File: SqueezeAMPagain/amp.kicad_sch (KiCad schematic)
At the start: 52 parts, among them U1 TAS5756M

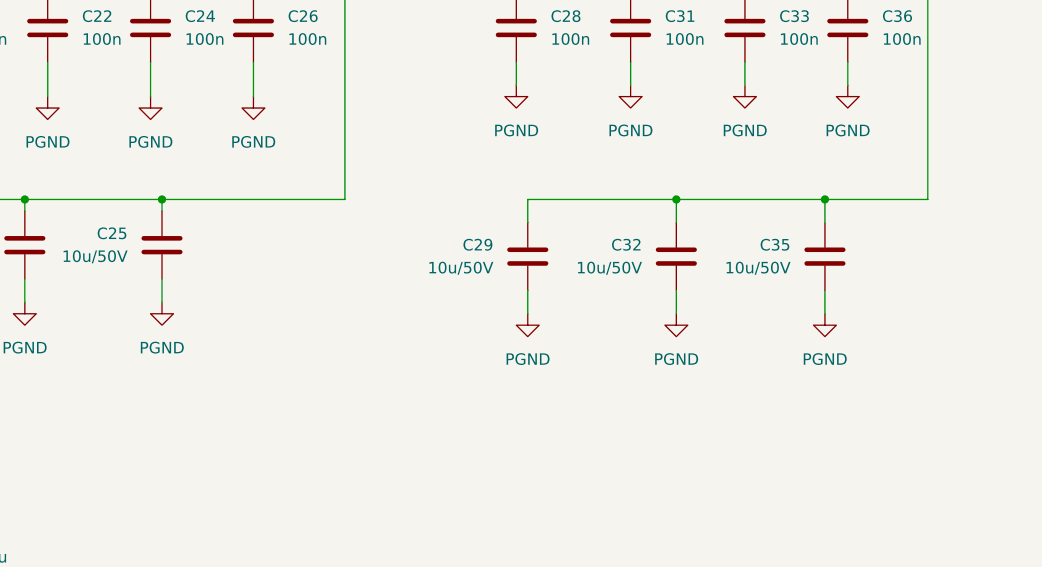
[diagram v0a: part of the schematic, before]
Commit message: Update SqueezeAMPagain.kicad_pcb, SqueezeAMPagain.kicad_prl, SqueezeAMPagain.kicad_pro, and 5 more files
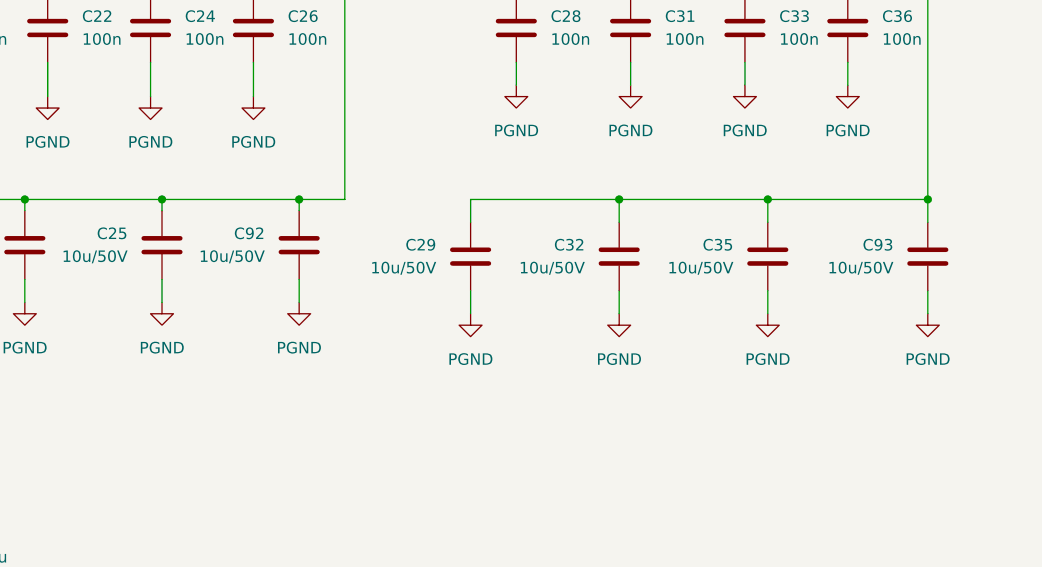
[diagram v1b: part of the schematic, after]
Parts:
- added C92, C93: 10u/50V, Capacitor_SMD:C_1206_3216Metric, symbol Device:C
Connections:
- net PGND: now also C92.2, C93.2
- net PVDD: now also C92.1, C93.1
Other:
- moved on the sheet: C29, C32, C35

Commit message: Update SqueezeAMPagain.kicad_pcb, SqueezeAMPagain.kicad_prl, SqueezeAMPagain.kicad_pro, and 11 more files
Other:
- title: Amplifier section -> SqueezeAMP_{again}
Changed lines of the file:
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@@
 	(paper "A4")
 	(title_block
-		(title "Amplifier section")
+		(title "SqueezeAMP_{again}")
+		(date "2024-08-23")
+		(rev "1.0")
 	)
 	(junction

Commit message: Update SqueezeAMPagain.kicad_pcb, SqueezeAMPagain.kicad_prl, SqueezeAMPagain.kicad_pro, and 4 more files
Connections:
- net +3.3V_{SW}: no longer C1.1, C3.1, U1.35 (CPVSS)
- new net: C1.1, C3.1, U1.35 (CPVSS)
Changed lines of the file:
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@@
 	)
 	(junction
-		(at 17.78 110.49)
-		(diameter 0)
-		(color 0 0 0 0)
-	)
-	(junction
 		(at 266.7 114.3)
 		(diameter 0)
@@
 					(unit 1)
 				)
-			)
-		)
-	)
-	(symbol
-		(lib_id "power:+3.3V")
-		(at 17.78 110.49 0)
-		(unit 1)
-		(exclude_from_sim no)
-		(in_bom yes)
-		(on_board yes)
-		(dnp no)
-		(fields_autoplaced yes)
-		(property "Reference" "#PWR03"
-			(at 17.78 114.3 0)
-			(effects
-				(font
-					(size 1.27 1.27)
-				)
-				(hide yes)
-			)
-		)
-		(property "Value" "+3.3V_{SW}"
-			(at 20.32 109.2199 0)
-			(effects
-				(font
-					(size 1.27 1.27)
-				)
-				(justify left)
-			)
-		)
-		(property "Footprint" ""
-			(at 17.78 110.49 0)
-			(effects
-				(font
-					(size 1.27 1.27)
-				)
-				(hide yes)
-			)
-		)
-		(property "Datasheet" ""
-			(at 17.78 110.49 0)
-			(effects
-				(font
-					(size 1.27 1.27)
-				)
-				(hide yes)
-			)
-		)
-		(property "Description" "Power symbol creates a global label with name \"+3.3V\""
-			(at 17.78 110.49 0)
-			(effects
-				(font
-					(size 1.27 1.27)
-				)
-				(hide yes)
-			)
-		)
-		(pin "1"
-		)
-		(instances
-			(project "SqueezeAMPagain"
-				(path "/3675160b-d9e5-490e-b506-2a7966e79ed0/07ac3e8e-f1ad-466e-8093-0e429e520f15"
-					(reference "#PWR03")
-					(unit 1)
-				)

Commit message: shrink
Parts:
- C12, C3, C4, C6, C9: footprint Capacitor_SMD:C_0603_1608Metric -> Capacitor_SMD:C_0402_1005Metric
- R4, R5, R6, R7, R8: footprint Resistor_SMD:R_0603_1608Metric -> Resistor_SMD:R_0402_1005Metric
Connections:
- net +3.3V: now also C2.1, C4.1, U1.31 (CPVDD)
- net +3.3V_{SW}: no longer C2.1, C4.1, U1.31 (CPVDD)
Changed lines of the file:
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@@
 	(wire
 		(pts
+			(xy 81.28 144.78) (xy 81.28 146.05)
+		)
+		(stroke
+			(width 0)
+			(type default)
+		)
+	)
+	(wire
+		(pts
 			(xy 257.81 146.05) (xy 257.81 148.59)
 		)
@@
 	)
 	(symbol
-		(lib_id "power:+3.3V")
-		(at 81.28 146.05 0)
-		(unit 1)
-		(exclude_from_sim no)
-		(in_bom yes)
-		(on_board yes)
-		(dnp no)
-		(property "Reference" "#PWR011"
-			(at 81.28 149.86 0)
-			(effects
-				(font
-					(size 1.27 1.27)
-				)
-				(hide yes)
-			)
-		)
-		(property "Value" "+3.3V"
-			(at 76.962 144.526 0)
-			(effects
-				(font
-					(size 1.27 1.27)
-				)
-			)
-		)
-		(property "Footprint" ""
-			(at 81.28 146.05 0)
-			(effects
-				(font
-					(size 1.27 1.27)
-				)
-				(hide yes)
-			)
-		)
-		(property "Datasheet" ""
-			(at 81.28 146.05 0)
-			(effects
-				(font
-					(size 1.27 1.27)
-				)
-				(hide yes)
-			)
-		)
-		(property "Description" "Power symbol creates a global label with name \"+3.3V\""
-			(at 81.28 146.05 0)
-			(effects
-				(font
-					(size 1.27 1.27)
-				)
-				(hide yes)
-			)
-		)
-		(pin "1"
-		)
-		(instances
-			(project "SqueezeAMPagain"
-				(path "/3675160b-d9e5-490e-b506-2a7966e79ed0/07ac3e8e-f1ad-466e-8093-0e429e520f15"
-					(reference "#PWR011")
-					(unit 1)
-				)
-			)
-		)
-	)
-	(symbol
 		(lib_id "power:GND1")
 		(at 160.02 157.48 0)
@@
 	)
 	(symbol
-		(lib_id "power:+3.3V")
-		(at 22.86 87.63 0)
-		(unit 1)
-		(exclude_from_sim no)
-		(in_bom yes)
-		(on_board yes)
-		(dnp no)
-		(fields_autoplaced yes)
-		(property "Reference" "#PWR04"
-			(at 22.86 91.44 0)
-			(effects
-				(font
-					(size 1.27 1.27)
-				)
-				(hide yes)
-			)
-		)
-		(property "Value" "+3.3V_{SW}"
-			(at 25.4 86.3599 0)
-			(effects
-				(font
-					(size 1.27 1.27)
-				)
-				(justify left)
-			)
-		)
-		(property "Footprint" ""
-			(at 22.86 87.63 0)
-			(effects
-				(font
-					(size 1.27 1.27)
-				)
-				(hide yes)
-			)
-		)
-		(property "Datasheet" ""
-			(at 22.86 87.63 0)
-			(effects
-				(font
-					(size 1.27 1.27)
-				)
-				(hide yes)
-			)
-		)
-		(property "Description" "Power symbol creates a global label with name \"+3.3V\""
-			(at 22.86 87.63 0)
-			(effects
-				(font
-					(size 1.27 1.27)
-				)
-				(hide yes)
-			)
-		)
-		(pin "1"
-		)
-		(instances
-			(project "SqueezeAMPagain"
-				(path "/3675160b-d9e5-490e-b506-2a7966e79ed0/07ac3e8e-f1ad-466e-8093-0e429e520f15"
-					(reference "#PWR04")
-					(unit 1)
-				)
-			)
-		)
-	)
-	(symbol
 		(lib_id "Device:C")
 		(at 113.03 157.48 0)
@@
 			)
 		)
-		(property "Footprint" "Capacitor_SMD:C_0603_1608Metric"
+		(property "Footprint" "Capacitor_SMD:C_0402_1005Metric"
 			(at 113.9952 161.29 0)
 			(effects
@@
 			)
 		)
-		(property "Footprint" "Resistor_SMD:R_0603_1608Metric"
+		(property "Footprint" "Resistor_SMD:R_0402_1005Metric"
 			(at 207.01 89.408 90)
 			(effects
@@
 			)
 		)
-		(property "Footprint" "Capacitor_SMD:C_0603_1608Metric"
+		(property "Footprint" "Capacitor_SMD:C_0402_1005Metric"
 			(at 39.0652 101.6 0)
 			(effects
@@
 			)
 		)
-		(property "Footprint" "Capacitor_SMD:C_0603_1608Metric"
+		(property "Footprint" "Capacitor_SMD:C_0402_1005Metric"
 			(at 100.0252 133.35 0)
 			(effects
@@
 			)
 		)
-		(property "Footprint" "Resistor_SMD:R_0603_1608Metric"
+		(property "Footprint" "Resistor_SMD:R_0402_1005Metric"
 			(at 24.892 66.04 90)
 			(effects
@@
 	)
 	(symbol
+		(lib_id "power:+3.3V")
+		(at 81.28 144.78 0)
+		(unit 1)
+		(exclude_from_sim no)
+		(in_bom yes)
+		(on_board yes)
+		(dnp no)
+		(fields_autoplaced yes)
+		(property "Reference" "#PWR011"
+			(at 81.28 148.59 0)
+			(effects
+				(font
+					(size 1.27 1.27)
+				)
+				(hide yes)
+			)
+		)
+		(property "Value" "+3.3V"
+			(at 81.28 139.7 0)
+			(effects
+				(font
+					(size 1.27 1.27)
+				)
+			)
+		)
+		(property "Footprint" ""
+			(at 81.28 144.78 0)
+			(effects
+				(font
+					(size 1.27 1.27)
+				)
+				(hide yes)
+			)
+		)
+		(property "Datasheet" ""
+			(at 81.28 144.78 0)
+			(effects
+				(font
+					(size 1.27 1.27)
+				)
+				(hide yes)
+			)
+		)
+		(property "Description" "Power symbol creates a global label with name \"+3.3V\""
+			(at 81.28 144.78 0)
+			(effects
+				(font
+					(size 1.27 1.27)
+				)
+				(hide yes)
+			)
+		)
+		(pin "1"
+		)
+		(instances
+			(project "SqueezeAMPagain"
+				(path "/3675160b-d9e5-490e-b506-2a7966e79ed0/07ac3e8e-f1ad-466e-8093-0e429e520f15"
+					(reference "#PWR011")
+					(unit 1)
+				)
+			)
+		)
+	)
+	(symbol
 		(lib_id "power:GND1")
 		(at 247.65 104.14 0)
@@
 			)
 		)
-		(property "Footprint" "Capacitor_SMD:C_0603_1608Metric"
+		(property "Footprint" "Capacitor_SMD:C_0402_1005Metric"
 			(at 68.2752 130.81 0)
 			(effects
@@
 			)
 		)
-		(property "Footprint" "Resistor_SMD:R_0603_1608Metric"
+		(property "Footprint" "Resistor_SMD:R_0402_1005Metric"
 			(at 43.942 66.04 90)
 			(effects
@@
 			)
 		)
-		(property "Footprint" "Resistor_SMD:R_0603_1608Metric"
+		(property "Footprint" "Resistor_SMD:R_0402_1005Metric"
 			(at 37.592 39.37 90)
 			(effects
@@
 			)
 		)
-		(property "Footprint" "Resistor_SMD:R_0603_1608Metric"
+		(property "Footprint" "Resistor_SMD:R_0402_1005Metric"
 			(at 33.782 66.04 90)
 			(effects
@@
 			)
 		)
-		(property "Footprint" "Capacitor_SMD:C_0603_1608Metric"
+		(property "Footprint" "Capacitor_SMD:C_0402_1005Metric"
 			(at 35.2552 132.08 0)
 			(effects
@@
 					(unit 1)
 				)
+			)
+		)
+	)
+	(symbol
+		(lib_id "power:+3.3V")
+		(at 22.86 87.63 0)
+		(unit 1)
+		(exclude_from_sim no)
+		(in_bom yes)
+		(on_board yes)
+		(dnp no)
+		(fields_autoplaced yes)
+		(property "Reference" "#PWR04"
+			(at 22.86 91.44 0)
+			(effects
+				(font
+					(size 1.27 1.27)
+				)
+				(hide yes)
+			)
+		)
+		(property "Value" "+3.3V"
+			(at 22.86 82.55 0)
+			(effects
+				(font
+					(size 1.27 1.27)
+				)
+			)
+		)
+		(property "Footprint" ""
+			(at 22.86 87.63 0)
+			(effects
+				(font
+					(size 1.27 1.27)
+				)
+				(hide yes)
+			)
+		)
+		(property "Datasheet" ""
+			(at 22.86 87.63 0)
+			(effects
+				(font
+					(size 1.27 1.27)
+				)
+				(hide yes)
+			)
+		)
+		(property "Description" "Power symbol creates a global label with name \"+3.3V\""
+			(at 22.86 87.63 0)
+			(effects
+				(font
+					(size 1.27 1.27)
+				)
+				(hide yes)
+			)
+		)
+		(pin "1"
+		)
+		(instances
+			(project ""
+				(path "/3675160b-d9e5-490e-b506-2a7966e79ed0/07ac3e8e-f1ad-466e-8093-0e429e520f15"
+					(reference "#PWR04")
+					(unit 1)
+				)

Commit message: v2
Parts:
- removed C26, C31, C36: 100n, Capacitor_SMD:C_0603_1608Metric, symbol Device:C
- removed C32: 10u/50V, Capacitor_SMD:C_1206_3216Metric, symbol Device:C
- added FB8, FB9: 600Ω@100MHz 500mA, Inductor_SMD:L_0805_2012Metric, symbol Device:FerriteBead_Small
- C11, C13, C14, C15, C16, C19: footprint Capacitor_THT:CP_Radial_D10.0mm_P5.00mm_P7.50mm -> Capacitor_THT:CP_Radial_D8.0mm_P3.50mm
- C24: value 100n -> 10u/50V; footprint Capacitor_SMD:C_0603_1608Metric -> Capacitor_SMD:C_1206_3216Metric
- R5, R7: footprint Resistor_SMD:R_0402_1005Metric -> Resistor_SMD:R_0603_1608Metric
- renumbered C92 to C27, C27 to C28, C28 to C30, C30 to C31, C33 to C34, C34 to C36, C37 to C38, C93 to C39
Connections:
- net +3.3V: now also FB8.1, FB9.1; no longer C2.1, C4.1, U1.31 (CPVDD)
- net +3.3V_{SW}: no longer names the net of C7.1, C9.1, U1.30 (DVDD)
- net +3.3V_{SW}: now also FB9.2
- new net: C2.1, C4.1, FB8.2, U1.31 (CPVDD)
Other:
- moved on the sheet: C1, C12, C2, C3, C34, C4, C5, C6, C8, FB1

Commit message: v2
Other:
- note added: "Ø max 8 mm Pitch 3,5 mm min 220u / 25V"
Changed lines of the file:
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@@
 (kicad_sch
-	(version 20231120)
+	(version 20250114)
 	(generator "eeschema")
-	(generator_version "8.0")
+	(generator_version "9.0")
 	(paper "A4")
 	(title_block
@@
 		(rev "1.0")
 	)
+	(text "Ø max 8 mm\nPitch 3,5 mm\nmin 220u / 25V"
+		(exclude_from_sim no)
+		(at 87.884 185.928 0)
+		(effects
+			(font
+				(size 1.27 1.27)
+			)
+			(justify left)
+		)
+	)
+	(text_box "R100 = 750k. R101 =150k --> 8x fSYNC, 26dBV"
+		(exclude_from_sim no)
+		(at 15.24 30.48 0)
+		(size 19.685 7.62)
+		(margins 0.9525 0.9525 0.9525 0.9525)
+		(stroke
+			(width 0)
+			(type default)
+		)
+		(fill
+			(type none)
+		)
+		(effects
+			(font
+				(size 1.27 1.27)
+			)
+			(justify left top)
+			(href "https://www.ti.com/document-viewer/TAS5756M/datasheet#detailed_description/SLAS9882285")
+		)
+	)
 	(junction
 		(at 99.06 152.4)
@@
 	(wire
 		(pts
-			(xy 82.55 151.13) (xy 82.55 152.4)
+			(xy 76.2 147.32) (xy 76.2 152.4)
 		)
 		(stroke
@@
 	(wire
 		(pts
-			(xy 82.55 152.4) (xy 87.63 152.4)
+			(xy 76.2 152.4) (xy 87.63 152.4)
 		)
 		(stroke
@@
 		)
 	)
-	(text_box "R100 = 750k. R101 =150k --> 8x fSYNC, 26dBV"
-		(exclude_from_sim no)
-		(at 15.24 30.48 0)
-		(size 19.685 7.62)
-		(stroke
-			(width 0)
-			(type default)
-		)
-		(fill
-			(type none)
-		)
-		(effects
-			(font
-				(size 1.27 1.27)
-			)
-			(justify left top)
-			(href "https://www.ti.com/document-viewer/TAS5756M/datasheet#detailed_description/SLAS9882285")
-		)
-	)
 	(label "GVDD_REG"
 		(at 53.34 31.75 180)
@@
 		(on_board yes)
 		(dnp no)
-		(fields_autoplaced yes)
 		(property "Reference" "#PWR017"
 			(at 68.58 125.73 0)
@@
 		)
 		(property "Value" "+3.3V"
-			(at 68.58 116.84 0)
+			(at 68.58 118.11 0)
 			(effects
 				(font
@@
 		(on_board yes)
 		(dnp no)
-		(fields_autoplaced yes)
 		(property "Reference" "FB9"
-			(at 76.1619 116.84 90)
+			(at 74.93 126.492 90)
 			(effects
 				(font
@@
 		)
 		(property "Value" "600Ω@100MHz 500mA"
-			(at 76.1619 119.38 90)
+			(at 73.66 128.524 90)
 			(effects
 				(font
@@
 	(symbol
 		(lib_id "power:+3.3V")
-		(at 82.55 151.13 0)
+		(at 76.2 147.32 0)
 		(unit 1)
 		(exclude_from_sim no)
@@
 		(fields_autoplaced yes)
 		(property "Reference" "#PWR016"
-			(at 82.55 154.94 0)
+			(at 76.2 151.13 0)
 			(effects
 				(font
@@
 		)
 		(property "Value" "+3.3V"
-			(at 82.55 146.05 0)
+			(at 76.2 142.24 0)
 			(effects
 				(font
@@
 		)
 		(property "Footprint" ""
-			(at 82.55 151.13 0)
+			(at 76.2 147.32 0)
 			(effects
 				(font
@@
 		)
 		(property "Datasheet" ""
-			(at 82.55 151.13 0)
+			(at 76.2 147.32 0)
 			(effects
 				(font
@@
 		)
 		(property "Description" "Power symbol creates a global label with name \"+3.3V\""
-			(at 82.55 151.13 0)
+			(at 76.2 147.32 0)
 			(effects
 				(font
@@
 		(at 238.76 77.47)
 		(size 24.13 5.08)
+		(exclude_from_sim no)
+		(in_bom yes)
+		(on_board yes)
+		(dnp no)
 		(stroke
 			(width 0.1524)
@@
 		(at 238.76 68.58)
 		(size 24.13 5.08)
+		(exclude_from_sim no)
+		(in_bom yes)
+		(on_board yes)
+		(dnp no)
 		(stroke
 			(width 0.1524)
@@
 		(at 238.76 59.69)
 		(size 24.13 5.08)
+		(exclude_from_sim no)
+		(in_bom yes)
+		(on_board yes)
+		(dnp no)
 		(stroke
 			(width 0.1524)
@@
 		(at 238.76 50.8)
 		(size 24.13 5.08)
+		(exclude_from_sim no)
+		(in_bom yes)
+		(on_board yes)
+		(dnp no)
 		(stroke
 			(width 0.1524)
